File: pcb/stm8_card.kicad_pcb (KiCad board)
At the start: 2 copper layers, 101.9 x 50.9 mm, 22 parts, among them J1 DEBUG HEADER, SW1 TL59AF100Q, SW2 TL59AF100Q, SW3 TL59AF100Q, SW4 TL3302AF260QG, U1 ER-OLED0.91-7, U2 STM8S103F3

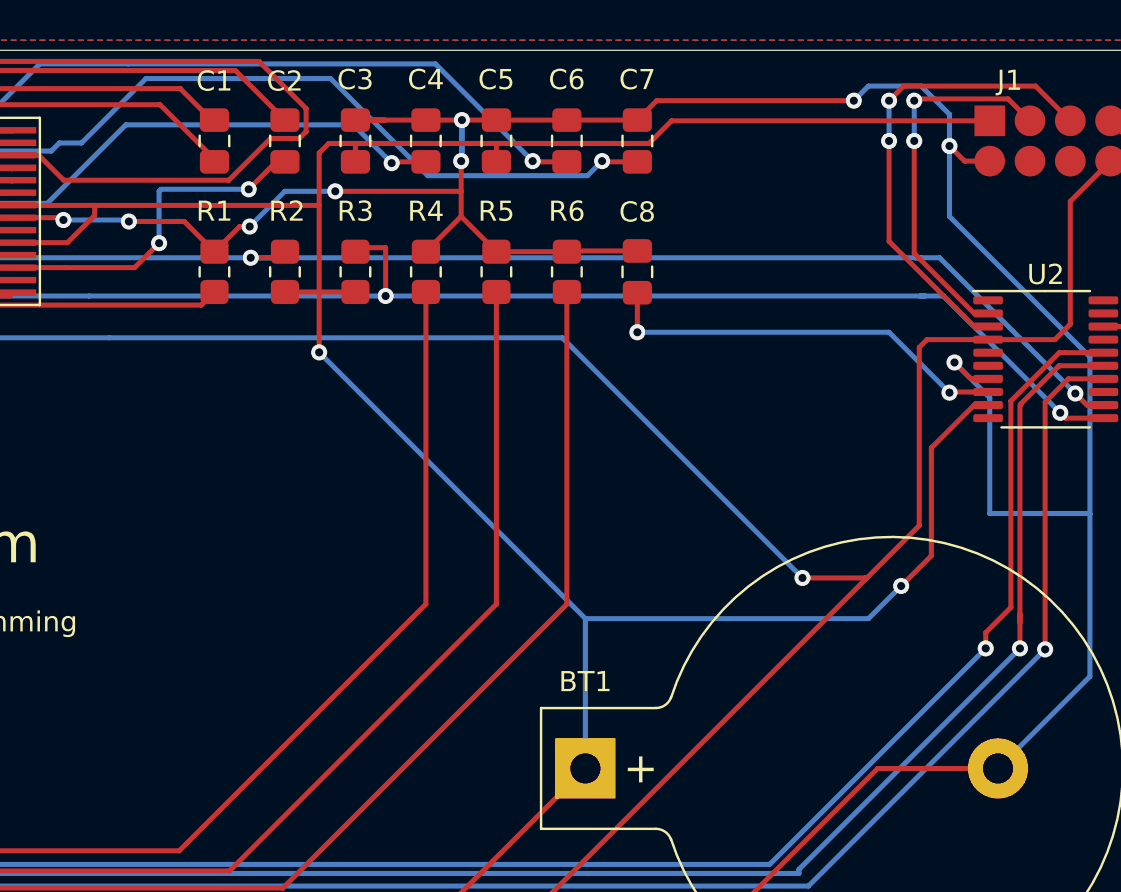
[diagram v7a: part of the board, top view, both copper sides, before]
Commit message: pcb removed some redundant vias
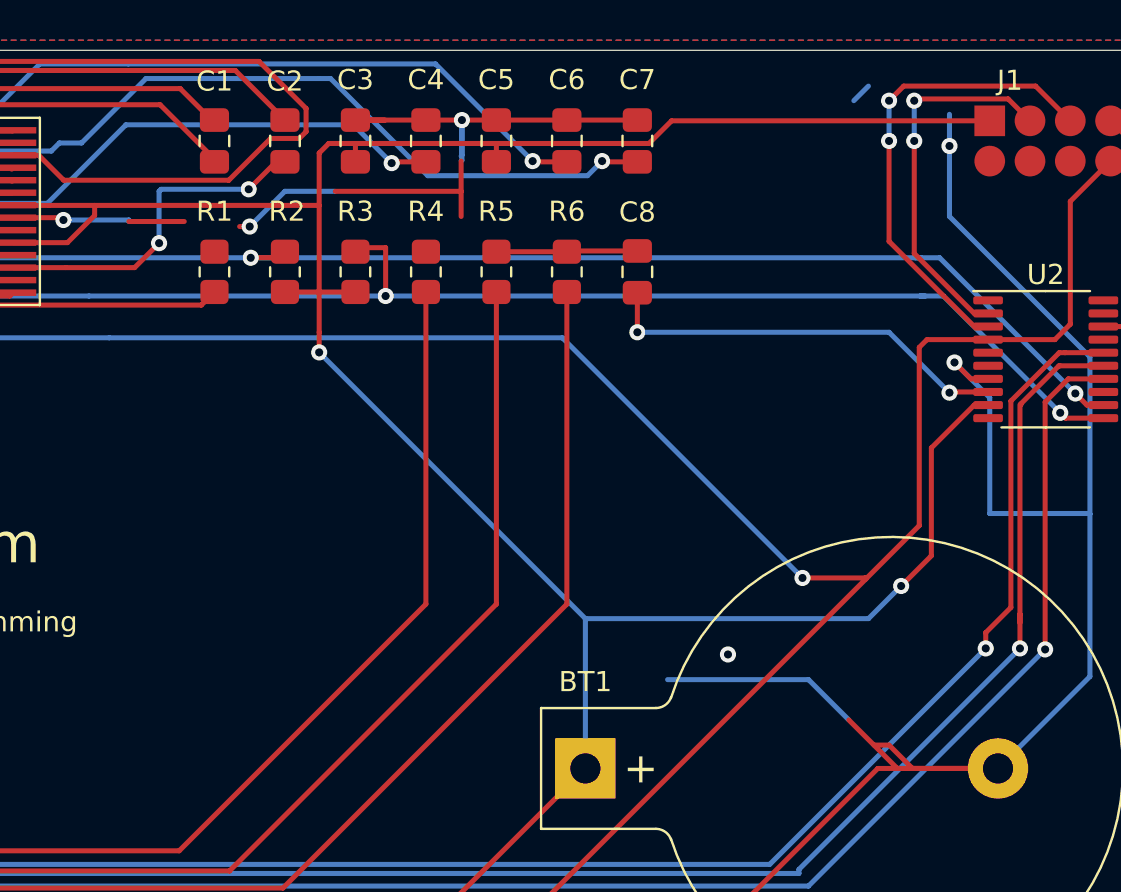
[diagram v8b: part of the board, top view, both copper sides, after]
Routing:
- net GND: track 152.0 -> 150.1 mm, vias 9 -> 6
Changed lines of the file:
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@@
     (47 F.CrtYd user)
     (48 B.Fab user)
-    (49 F.Fab user)
+    (49 F.Fab user hide)
   )
   (setup
@@
   (segment (start 242.7875 104.9625) (end 242.7875 106.7125) (width 0.25) (layer B.Cu) (net 1))
   (segment (start 242.7875 106.7125) (end 242.75 106.75) (width 0.25) (layer B.Cu) (net 1))
-  (via (at 242.75 107) (size 0.8) (drill 0.4) (layers F.Cu B.Cu) (net 1))
   (segment (start 242.7875 106.9625) (end 242.75 107) (width 0.25) (layer B.Cu) (net 1))
   (segment (start 242.7875 104.9625) (end 242.7875 106.9625) (width 0.25) (layer B.Cu) (net 1))
@@
   (segment (start 222.885 109.81) (end 223 109.925) (width 0.25) (layer F.Cu) (net 1))
   (segment (start 220.5 109.81) (end 222.885 109.81) (width 0.25) (layer F.Cu) (net 1))
-  (segment (start 242.75 109.75) (end 241 111.5) (width 0.25) (layer F.Cu) (net 1))
   (segment (start 242.7875 104.9625) (end 241 104.9625) (width 0.25) (layer F.Cu) (net 1))
   (segment (start 241 104.9625) (end 237.5 104.9625) (width 0.25) (layer F.Cu) (net 1))
   (segment (start 244.5 104.9625) (end 248 104.9625) (width 0.25) (layer F.Cu) (net 1))
   (segment (start 251.5 104.9625) (end 248 104.9625) (width 0.25) (layer F.Cu) (net 1))
-  (segment (start 244.5 111.5) (end 242.75 109.75) (width 0.25) (layer F.Cu) (net 1))
   (segment (start 248 111.5) (end 244.5 111.5) (width 0.25) (layer F.Cu) (net 1))
   (segment (start 248.0375 111.4625) (end 248 111.5) (width 0.25) (layer F.Cu) (net 1))
   (segment (start 251.5 111.4625) (end 248.0375 111.4625) (width 0.25) (layer F.Cu) (net 1))
-  (via (at 236.5 108.5) (size 0.8) (drill 0.4) (layers F.Cu B.Cu) (net 1))
   (segment (start 242.75 108.5) (end 236.5 108.5) (width 0.25) (layer F.Cu) (net 1))
   (segment (start 242.75 107) (end 242.75 108.5) (width 0.25) (layer F.Cu) (net 1))
@@
   (segment (start 236.5 108.5) (end 234 108.5) (width 0.25) (layer B.Cu) (net 1))
   (segment (start 223 109.925) (end 226.25 109.925) (width 0.25) (layer B.Cu) (net 1))
-  (via (at 226.25 110) (size 0.8) (drill 0.4) (layers F.Cu B.Cu) (net 1))
   (segment (start 226.25 109.925) (end 226.25 110) (width 0.25) (layer B.Cu) (net 1))
   (segment (start 226.25 110) (end 229 110) (width 0.25) (layer F.Cu) (net 1))
   (segment (start 234 108.5) (end 232.25 110.25) (width 0.25) (layer B.Cu) (net 1))
-  (segment (start 231.75 110.25) (end 230.5 111.5) (width 0.25) (layer F.Cu) (net 1))
   (segment (start 232.25 110.25) (end 231.75 110.25) (width 0.25) (layer F.Cu) (net 1))
   (via (at 232.25 110.25) (size 0.8) (drill 0.4) (layers F.Cu B.Cu) (net 1))
-  (segment (start 229 110) (end 230.5 111.5) (width 0.25) (layer F.Cu) (net 1))
   (via (at 267 106.25) (size 0.8) (drill 0.4) (layers F.Cu B.Cu) (net 1))
-  (segment (start 267.75 107) (end 267 106.25) (width 0.25) (layer F.Cu) (net 1))
-  (segment (start 269 107) (end 267.75 107) (width 0.25) (layer F.Cu) (net 1))
   (segment (start 262.975001 103.274999) (end 262.25 104) (width 0.25) (layer B.Cu) (net 1))
-  (segment (start 265.598001 103.274999) (end 262.975001 103.274999) (width 0.25) (layer B.Cu) (net 1))
-  (via (at 262.25 104) (size 0.8) (drill 0.4) (layers F.Cu B.Cu) (net 1))
-  (segment (start 267 104.676998) (end 265.598001 103.274999) (width 0.25) (layer B.Cu) (net 1))
   (segment (start 267 106.25) (end 267 104.676998) (width 0.25) (layer B.Cu) (net 1))
   (segment (start 268.065 117.815) (end 267.25 117) (width 0.25) (layer F.Cu) (net 1))
   (via (at 267.25 117) (size 0.8) (drill 0.4) (layers F.Cu B.Cu) (net 1))
   (segment (start 268.9175 117.815) (end 268.065 117.815) (width 0.25) (layer F.Cu) (net 1))
-  (segment (start 252.4625 104) (end 251.5 104.9625) (width 0.25) (layer F.Cu) (net 1))
-  (segment (start 262.25 104) (end 252.4625 104) (width 0.25) (layer F.Cu) (net 1))
   (segment (start 267 106.25) (end 267 109.75) (width 0.25) (layer B.Cu) (net 1))
   (segment (start 273.975001 132.594999) (end 269.41 137.16) (width 0.25) (layer B.Cu) (net 1))
@@
   (segment (start 263.44 137.16) (end 252 148.6) (width 0.25) (layer F.Cu) (net 1))
   (segment (start 269.41 137.16) (end 263.44 137.16) (width 0.25) (layer F.Cu) (net 1))
+  (segment (start 251.5 111.4625) (end 251.4625 111.4625) (width 0.25) (layer F.Cu) (net 1))
+  (segment (start 251.5 111.4625) (end 251.5375 111.4625) (width 0.25) (layer F.Cu) (net 1))
+  (segment (start 251.5 104.9625) (end 251.4625 104.9625) (width 0.25) (layer F.Cu) (net 1))
+  (segment (start 248 104.9625) (end 248.0375 104.9625) (width 0.25) (layer F.Cu) (net 1))
+  (segment (start 248 104.9625) (end 247.9625 104.9625) (width 0.25) (layer F.Cu) (net 1))
+  (segment (start 269.41 137.16) (end 265.16 137.16) (width 0.25) (layer F.Cu) (net 1))
+  (segment (start 265.16 137.16) (end 264 136) (width 0.25) (layer F.Cu) (net 1))
+  (segment (start 264 136) (end 263.25 136) (width 0.25) (layer F.Cu) (net 1))
+  (segment (start 264.41 137.16) (end 262 134.75) (width 0.25) (layer F.Cu) (net 1))
+  (segment (start 269.41 137.16) (end 264.41 137.16) (width 0.25) (layer F.Cu) (net 1))
+  (via (at 256 131.5) (size 0.8) (drill 0.4) (layers F.Cu B.Cu) (net 1))
+  (segment (start 260 132.75) (end 253 132.75) (width 0.25) (layer B.Cu) (net 1))
+  (segment (start 262 134.75) (end 260 132.75) (width 0.25) (layer B.Cu) (net 1))
   (segment (start 253.2 105) (end 252.07501 106.12499) (width 0.25) (layer F.Cu) (net 2))
   (segment (start 252.07501 106.12499) (end 245.41251 106.12499) (width 0.25) (layer F.Cu) (net 2))
@@
   (via (at 235.7 116.5) (size 0.8) (drill 0.4) (layers F.Cu B.Cu) (net 2))
   (segment (start 248.92 129.72) (end 235.7 116.5) (width 0.25) (layer B.Cu) (net 2))
-  (segment (start 235.7 116.5) (end 235.7 113.5) (width 0.25) (layer F.Cu) (net 2))
   (segment (start 264.6 128.1) (end 266.1 126.6) (width 0.25) (layer F.Cu) (net 2))
   (segment (start 268.228942 119.115) (end 268.9175 119.115) (width 0.25) (layer F.Cu) (net 2))
@@
   (segment (start 208 147.5) (end 238.58 147.5) (width 0.25) (layer F.Cu) (net 2))
   (segment (start 199 147.5) (end 208 147.5) (width 0.25) (layer F.Cu) (net 2))
+  (segment (start 235.7 115.5) (end 235.7 113.5) (width 0.25) (layer F.Cu) (net 2))
+  (segment (start 235.7 115.5) (end 235.7 116.75) (width 0.25) (layer F.Cu) (net 2))
   (segment (start 230.5 104.9625) (end 230.3625 104.9625) (width 0.25) (layer F.Cu) (net 3))
   (segment (start 230.3625 104.9625) (end 228.8 103.4) (width 0.25) (layer F.Cu) (net 3))
